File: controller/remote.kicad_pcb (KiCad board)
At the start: 2 copper layers, 69 x 58.7 mm, 41 parts, among them J1 Conn_01x03, J2 Debug, J3 Conn_01x06, J4 Conn_01x08, J5 Conn_01x08, J6 Jumper, Q1 MMBT3904, Q2 MMBT3904, SW1 SW_SPST, SW2 SW_SPST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

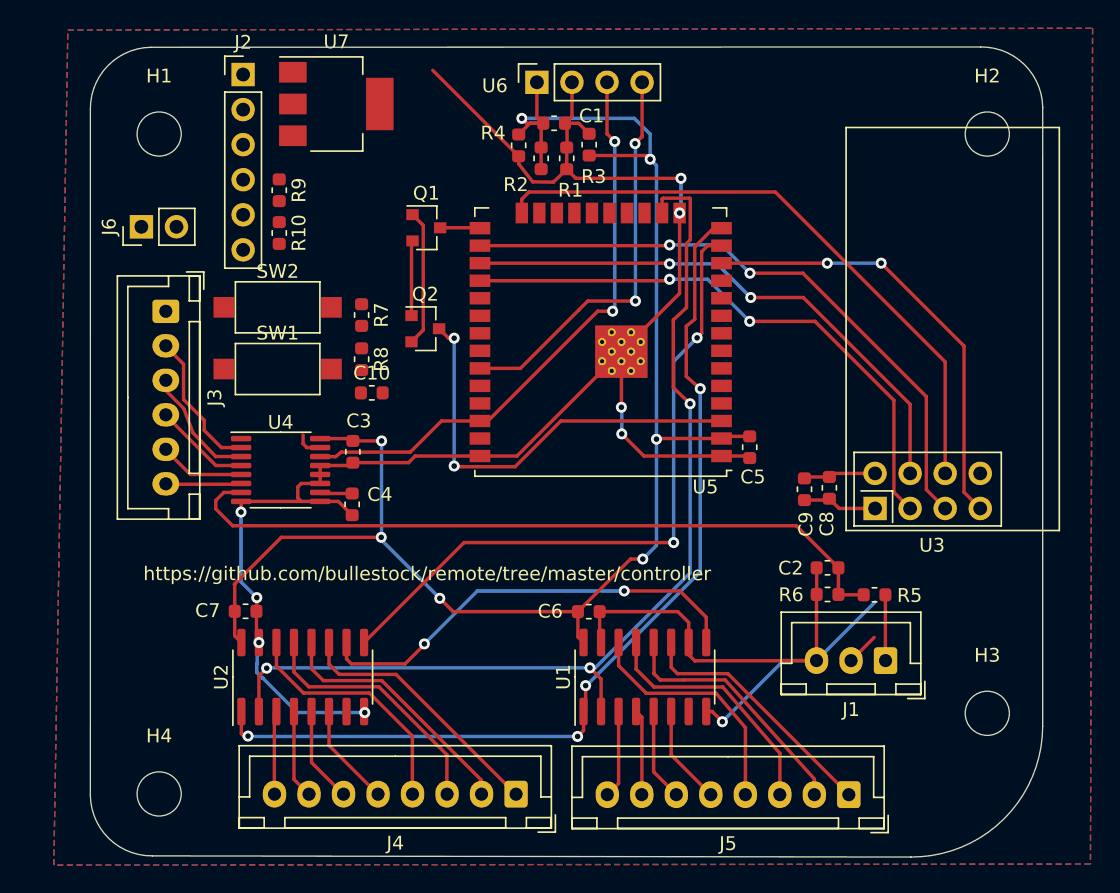
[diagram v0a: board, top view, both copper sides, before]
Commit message: Finish routing.
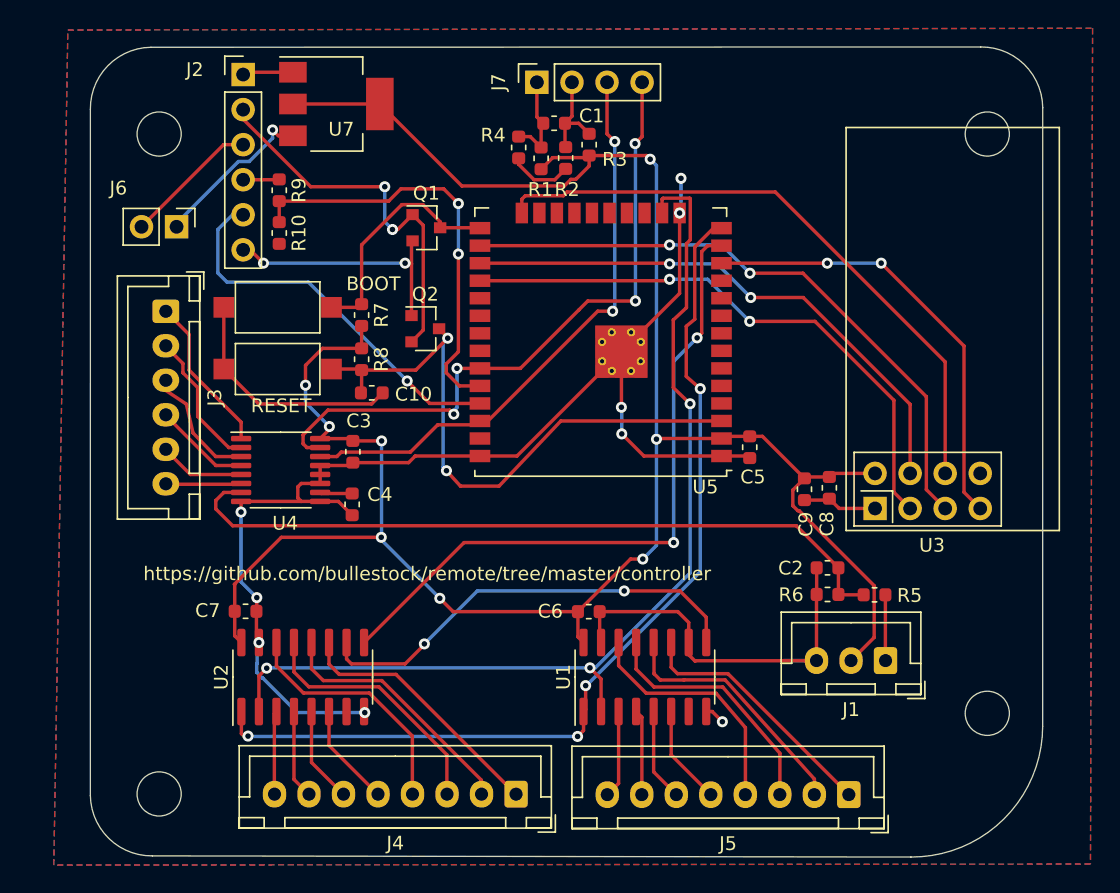
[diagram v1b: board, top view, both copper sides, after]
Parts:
- removed U6: MC130VX, Remote:Display_OLED_4pin_I2C
- added J7: MC130VX, Connector_PinSocket_2.54mm:PinSocket_1x04_P2.54mm_Vertical, F.Cu at (293.4, 95.2)
- moved J6 2.55 mm to (267.3, 105.7), turned to -90 degrees
- moved R1 1.85 mm to (293.7, 100.8)
- moved R2 1.78 mm to (295.5, 100.7)
- moved R4 0.15 mm to (292.0, 100.0)
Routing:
- net +3V3: track 123.6 -> 163.1 mm, vias 7 -> 8
- net MCU_RX0: track 0.00 -> 30.8 mm, vias 0 -> 2
- net MCU_TX0: track 0.00 -> 28.3 mm, vias 0 -> 1
- net RTS: track 10.0 -> 28.2 mm, vias 0 -> 2
- net GND: track 170.3 -> 152.9 mm
- net SDA: track 31.3 -> 48.2 mm, vias 2 -> 4
- net ~{BOOT}: track 2.89 -> 17.3 mm
- net ~{RESET}: track 31.4 -> 44.3 mm
- net DTR: track 5.45 -> 18.1 mm, vias 0 -> 2
- net +5V: track 0.00 -> 12.0 mm, vias 0 -> 1
- net Net-(J3-Pin_1): track 0.00 -> 11.5 mm
- net Net-(J2-Pin_3): track 0.00 -> 9.82 mm
- net Net-(J7-Pin_2): track 0.00 -> 6.99 mm
- net Net-(J7-Pin_1): track 0.00 -> 6.94 mm
- net Net-(J2-Pin_4): track 0.00 -> 2.63 mm
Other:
- board text added: "BOOT"
- board text added: "RESET"

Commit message: Add nRF mounting screw.
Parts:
- added H5: MountingHole, MountingHole:MountingHole_2.2mm_M2, F.Cu at (321.7, 108.6)
- moved C8 0.81 mm to (315.4, 124.7)
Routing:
- net GND: track 152.9 -> 155.4 mm
- net MISO: track 32.3 -> 31.4 mm
- net MOSI: track 45.1 -> 44.3 mm
